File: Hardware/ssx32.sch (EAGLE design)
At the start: 74 parts, among them IC1 PIC18LF45K20, IC2 FT232RL, IC3 TXB0108PW, IC4 TXB0108PW, IC5 TXB0108PW, IC6 TXB0108PW, IC7 3V3Regler, X1 8, X10 1, X11 19, X12 16, X13 15, X14 14, X15 13, X16 12, X17 11, X18 10, X19 9, X20 20, X21 21, X22 22, X23 23, X24 24, X25 25, X26 26, X27 27, X28 28, X29 29, X3 17, X30 30, X31 31, X32 32, X33 1751248, X34 18, X35 USB, X4 7, X5 6, X6 5, X7 4, X8 3, X9 2

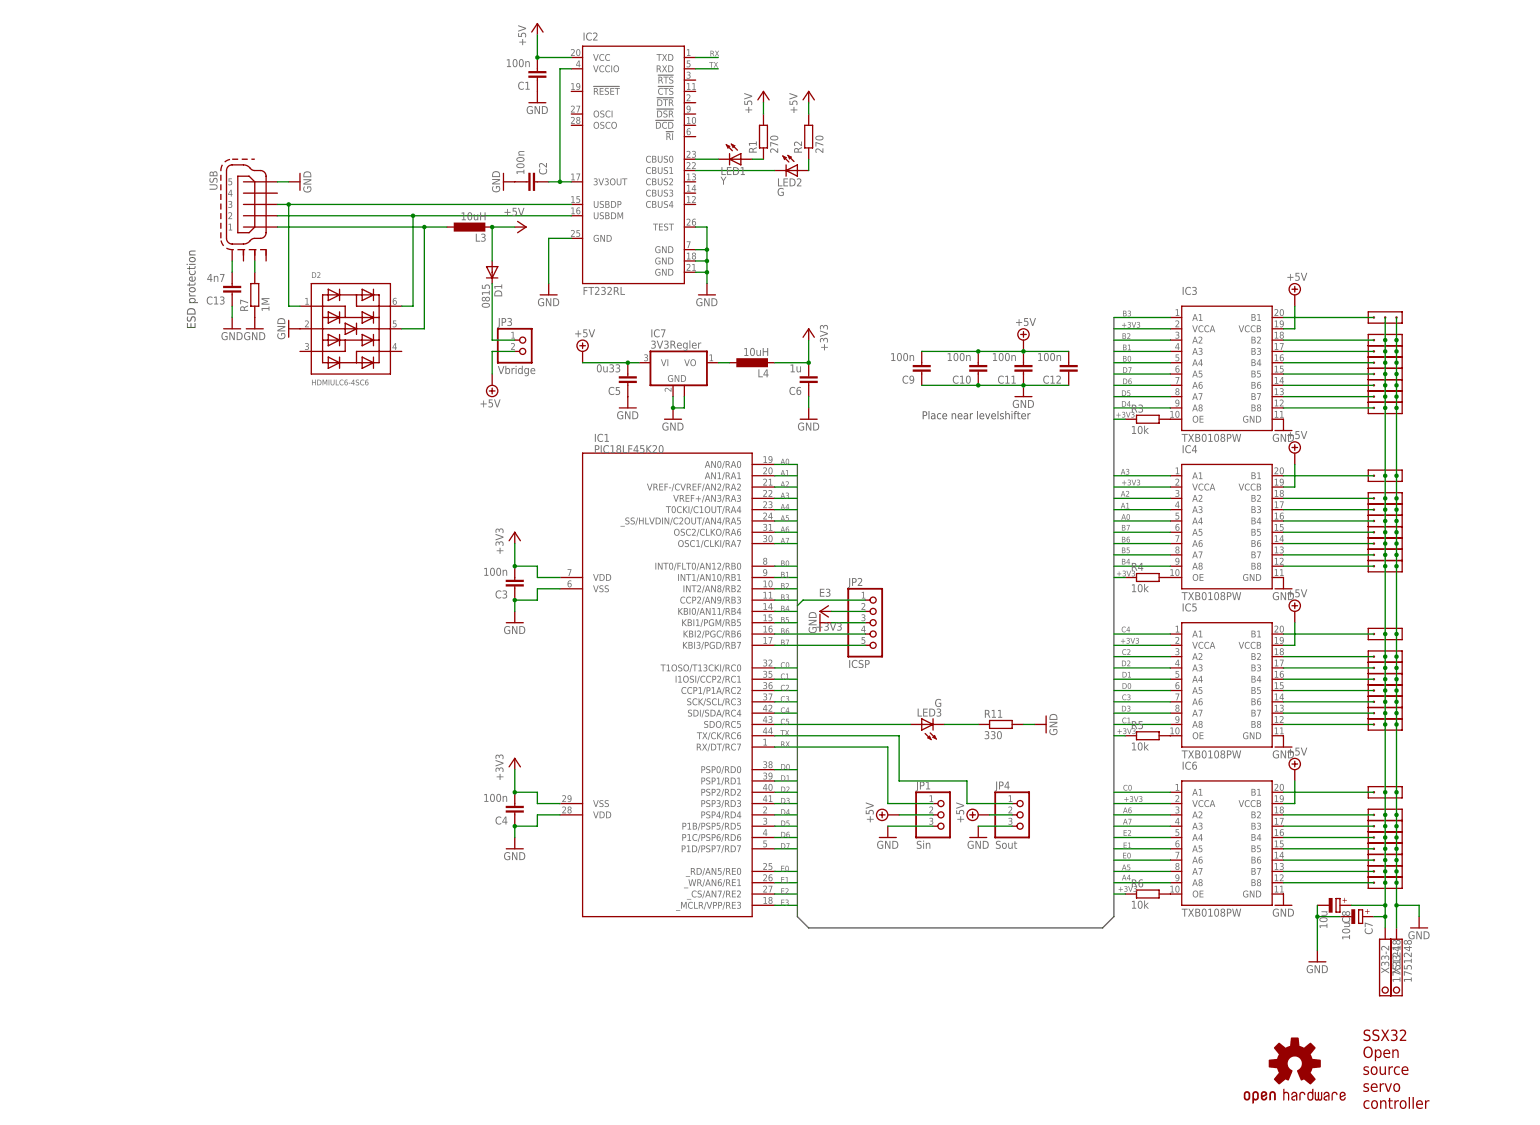
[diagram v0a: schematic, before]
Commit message: Changed Board
Added polyfuse
Changed component values
Replaced some components for easier PnP
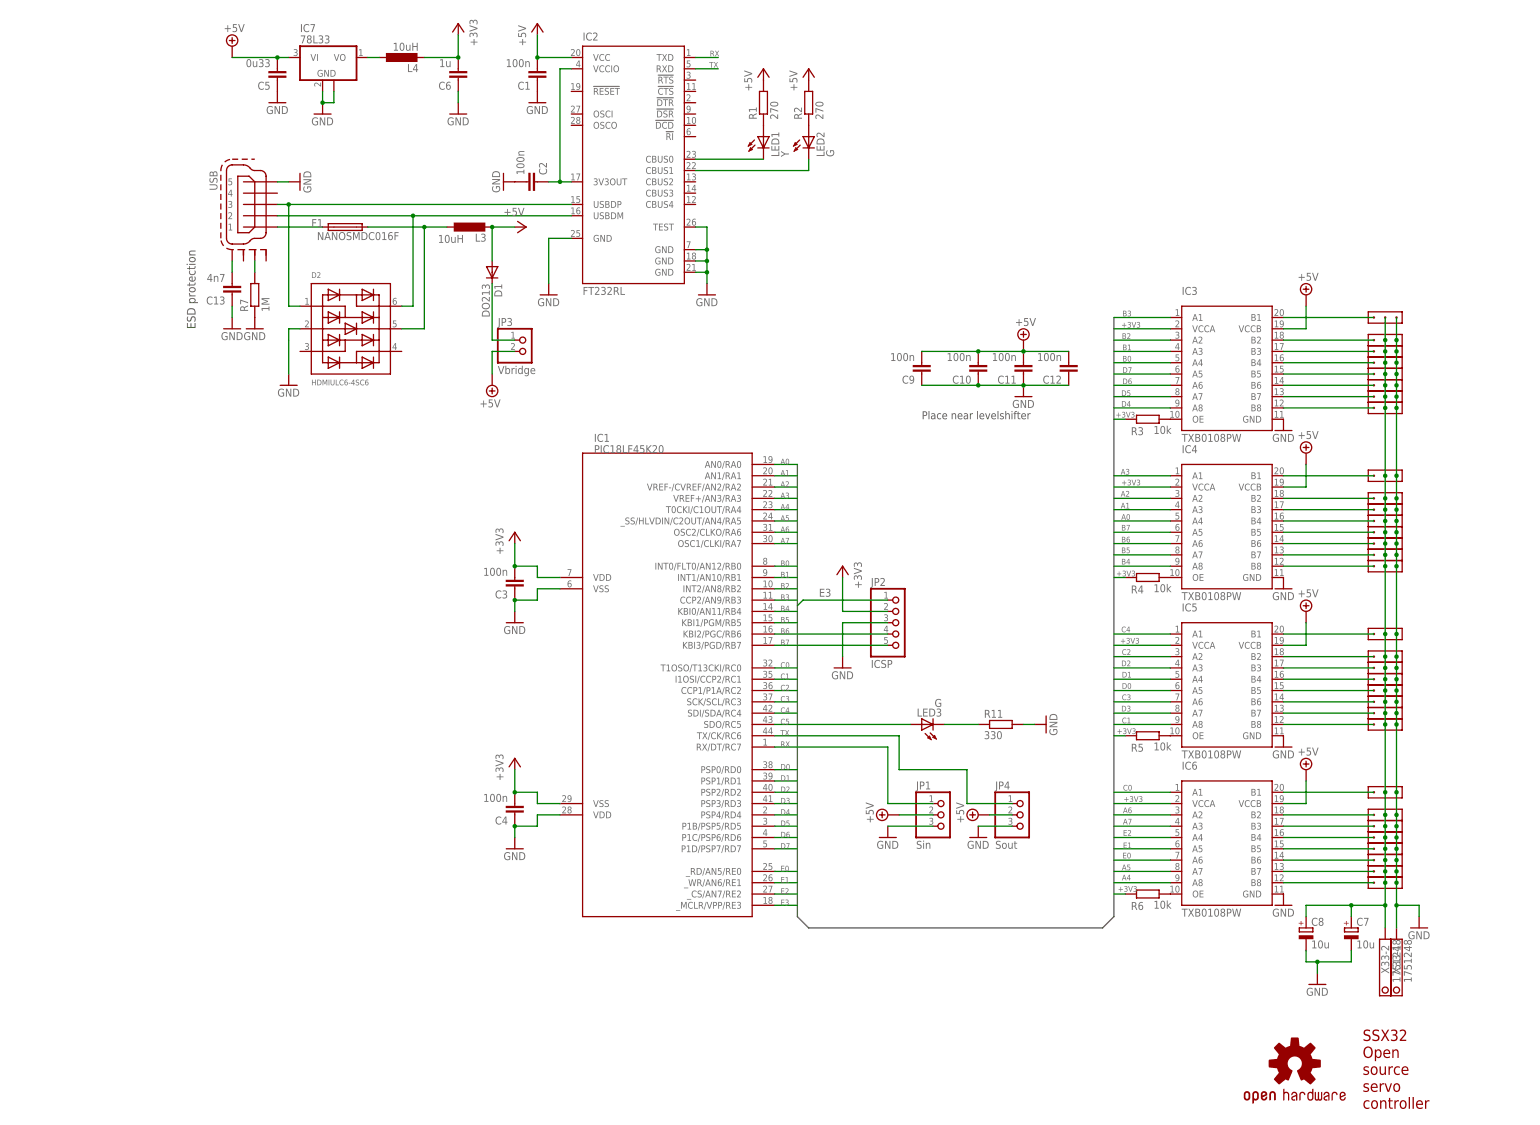
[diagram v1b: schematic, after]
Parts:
- added F1: NANOSMDC016F, fuse:NANOSMDC016F
- D1: value 0815 -> DO213; device diode:DIODE-MICROMELF-R -> diode:DIODE-MINIMELF
- IC7: value 3V3Regler -> 78L33
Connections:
- new net N$2: F1.1, X35G$1.1
- net N$51: now also F1.2; no longer X35G$1.1
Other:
- moved on the sheet: C5, C6, C7, C8, IC7, JP2, L4, LED1, LED2, R1, R2

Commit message: Error correction
Changed missconnected PIC power supply
Added protection for serial signals
Changed inductors to ferrite beads
Removed voltage select jumper
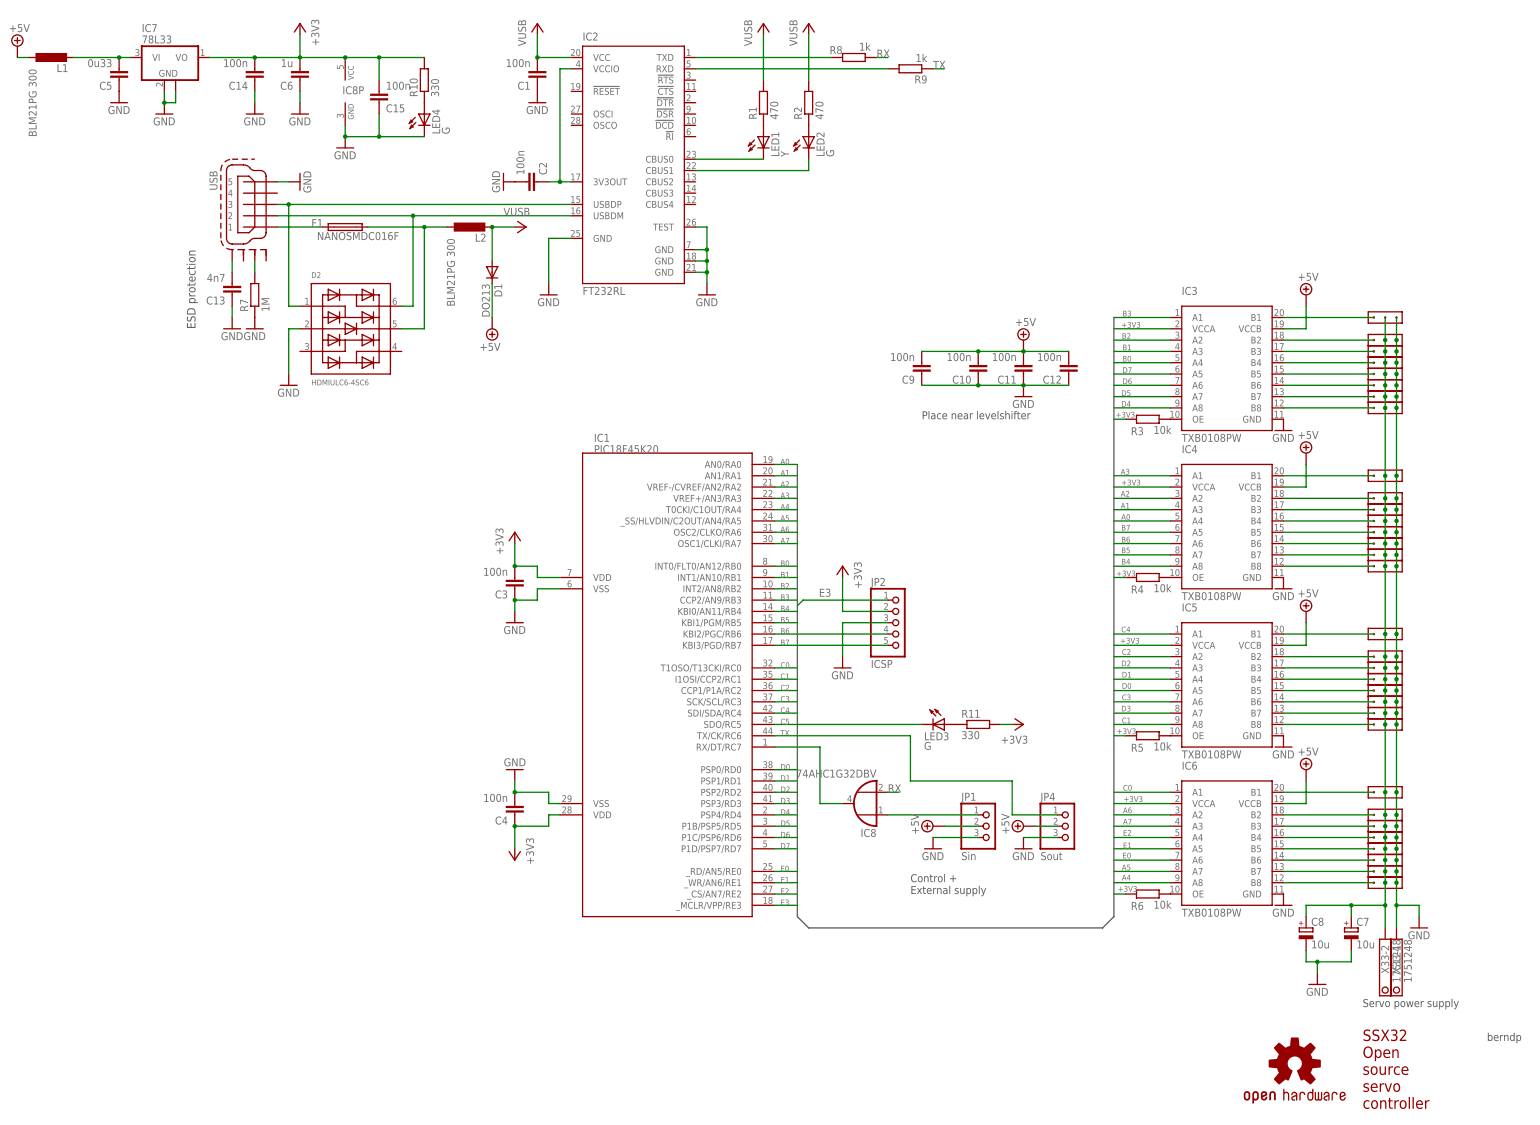
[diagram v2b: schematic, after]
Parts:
- removed JP3: Vbridge, pinhead:PINHD-1X2
- removed L4: 10uH, rcl:L-EU0805
- added C14, C15: 100n, rcl:C-EUC0603
- added IC8: 74AHC1G32DBV, 74xx-little-de:74AHC1G32DBV
- added L1: BLM21PG 300, rcl:L-EU0805
- added LED4: G, led:LEDCHIPLED_0603
- added R10: 330, rcl:R-EU_R0603
- added R8, R9: 1k, rcl:R-EU_R0603
- IC1: value PIC18LF45K20 -> PIC18F45K20
- L2: value 10uH -> BLM21PG 300
- R1, R2: value 270 -> 470
- renumbered L3 to L2
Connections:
- new net N$52: IC2.RXD, R9.2
- new net N$53: IC2.TXD, R8.2
- new net N$54: IC8A.I0, JP1.1
- new net N$55: LED4.A, R10.1
- net +3V3: now also C14.2, C15.2, C4.1, IC1.VDD@1, IC7.VO, IC8P.VCC, R10.2, R11.2; no longer C4.2, IC1.VSS@1, L4.2
- net +UB: now also D1.C, L1.1; no longer C5.2, IC7.VI, JP3.2
- net C5: now also LED3.C; no longer LED3.A
- net GND: now also C14.1, C15.1, C4.2, IC1.VSS@1, IC8P.GND, LED4.C; no longer C4.1, IC1.VDD@1, R11.2
- net N$45: now also LED3.A; no longer LED3.C
- net N$46: now also C5.2, IC7.VI, L1.2; no longer D1.C, JP3.1
- net N$48: now also IC1.RX/DT/RC7, IC8A.O; no longer IC7.VO, L4.1
- net RX: now also IC8A.I1, R8.1; no longer IC1.RX/DT/RC7, IC2.TXD, JP1.1
- net TX: now also R9.1; no longer IC2.RXD
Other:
- note added: "Control + External supply"
- note added: "Servo power supply"
- note added: "berndp"
- moved on the sheet: C5, C6, IC7, JP1, JP4, LED3, R11

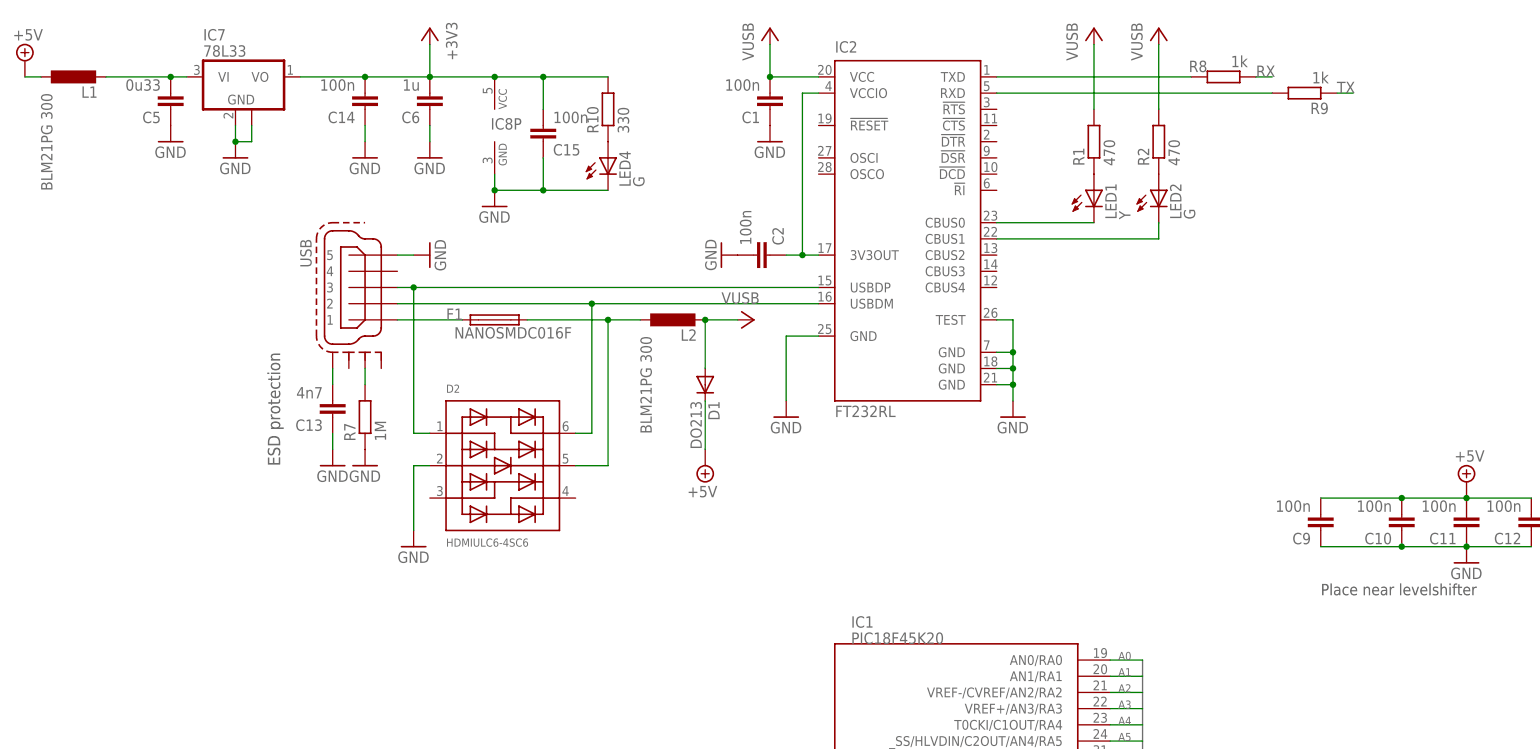
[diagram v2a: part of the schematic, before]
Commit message: Added Plane
Added groundplane
Increased servo VCC trace width
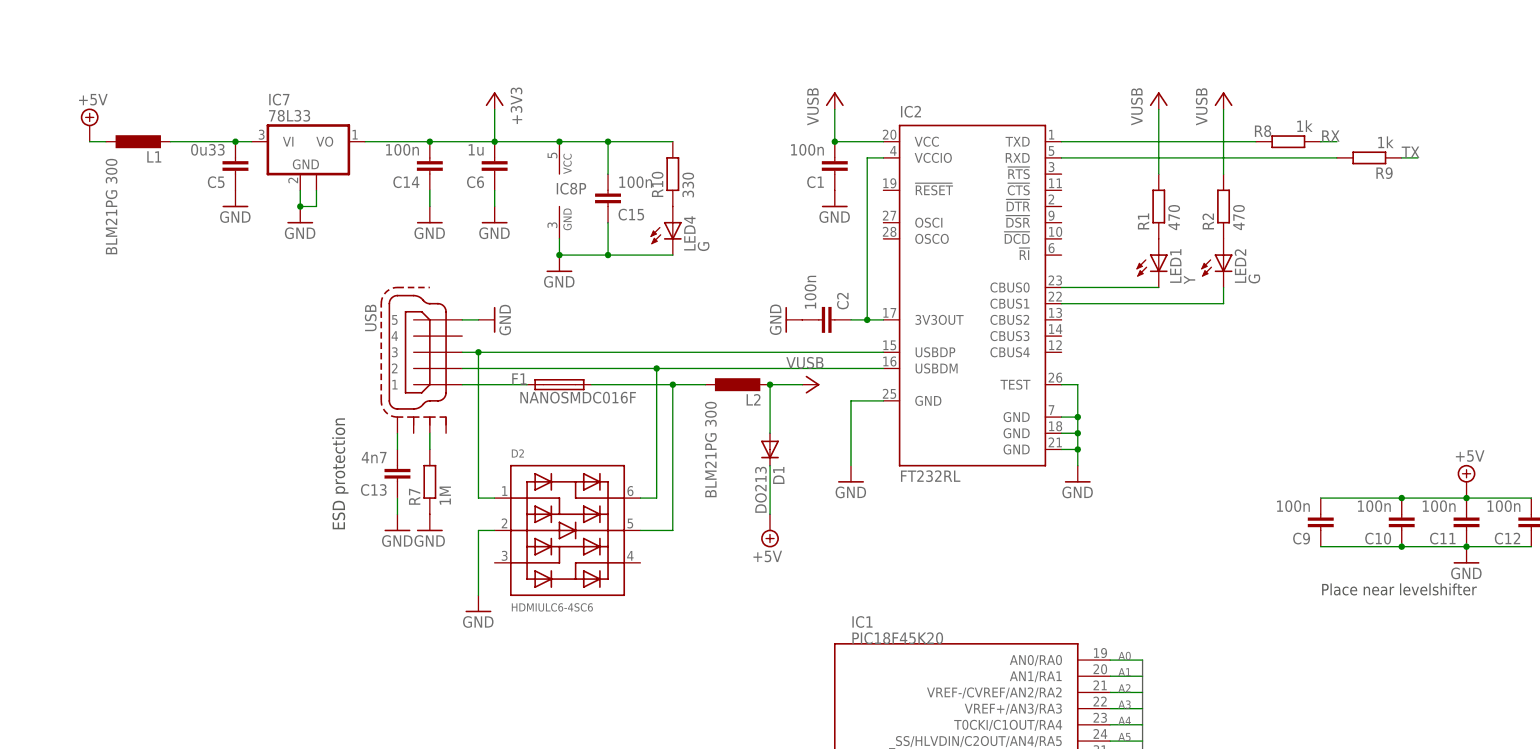
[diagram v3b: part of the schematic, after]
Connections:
- net N$42 renamed VSERVO
- net N$7 renamed VPORT
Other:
- moved on the sheet: C1, C13, C14, C15, C2, C5, C6, D1, D2, F1, IC2, IC7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

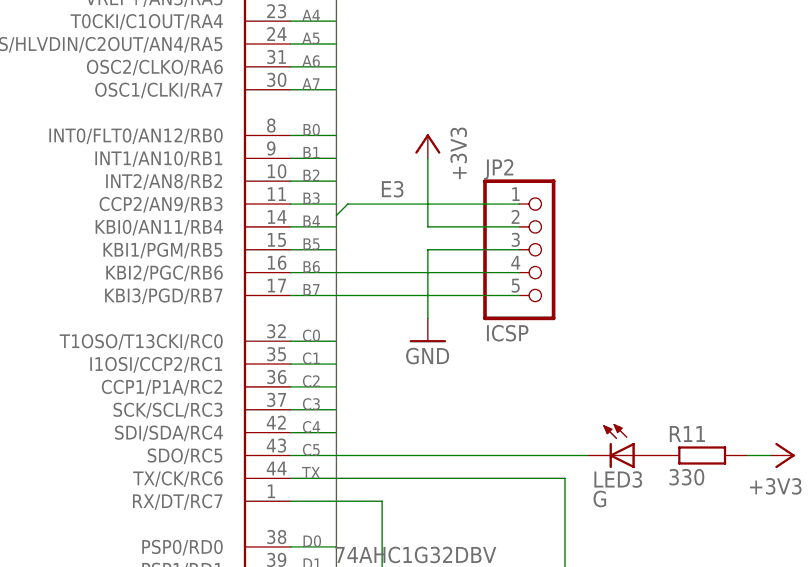
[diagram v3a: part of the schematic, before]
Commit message: Fixed ICSP interface
Fixed missconnected ICSP interface
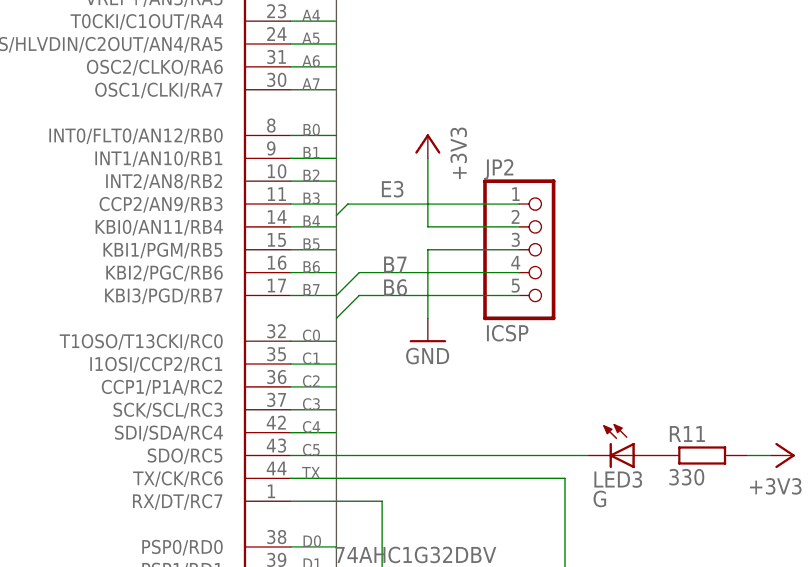
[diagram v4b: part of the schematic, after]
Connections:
- net B6: now also JP2.5; no longer JP2.4
- net B7: now also JP2.4; no longer JP2.5
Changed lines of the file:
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@@
 <net name="B6" class="0">
 <segment>
-<wire x1="142.24" y1="109.22" x2="167.64" y2="109.22" width="0.1524" layer="91"/>
+<wire x1="142.24" y1="109.22" x2="147.32" y2="109.22" width="0.1524" layer="91"/>
 <label x="143.51" y="109.22" size="1.27" layer="95"/>
 <pinref part="IC1" gate="G$2" pin="KBI2/PGC/RB6"/>
-<pinref part="JP2" gate="A" pin="4"/>
 </segment>
 <segment>
@@
 <pinref part="IC4" gate="G$1" pin="A6"/>
 </segment>
+<segment>
+<pinref part="JP2" gate="A" pin="5"/>
+<wire x1="167.64" y1="106.68" x2="149.86" y2="106.68" width="0.1524" layer="91"/>
+<wire x1="149.86" y1="106.68" x2="147.32" y2="104.14" width="0.1524" layer="91"/>
+<label x="152.4" y="106.68" size="1.778" layer="95"/>
+</segment>
 </net>
 <net name="B7" class="0">
 <segment>
-<wire x1="142.24" y1="106.68" x2="167.64" y2="106.68" width="0.1524" layer="91"/>
+<wire x1="142.24" y1="106.68" x2="147.32" y2="106.68" width="0.1524" layer="91"/>
 <label x="143.51" y="106.68" size="1.27" layer="95"/>
 <pinref part="IC1" gate="G$2" pin="KBI3/PGD/RB7"/>
-<pinref part="JP2" gate="A" pin="5"/>
 </segment>
 <segment>
@@
 <pinref part="IC4" gate="G$1" pin="A5"/>
 </segment>
+<segment>
+<pinref part="JP2" gate="A" pin="4"/>
+<wire x1="167.64" y1="109.22" x2="149.86" y2="109.22" width="0.1524" layer="91"/>
+<wire x1="149.86" y1="109.22" x2="147.32" y2="106.68" width="0.1524" layer="91"/>
+<label x="152.4" y="109.22" size="1.778" layer="95"/>
+</segment>
 </net>
